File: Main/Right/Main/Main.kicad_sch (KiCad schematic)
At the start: 44 parts, among them SW1 RotaryEncoder_Switch_MP, SW2 Switch, U1 Arduino_Pro_Micro, U2 TRRS

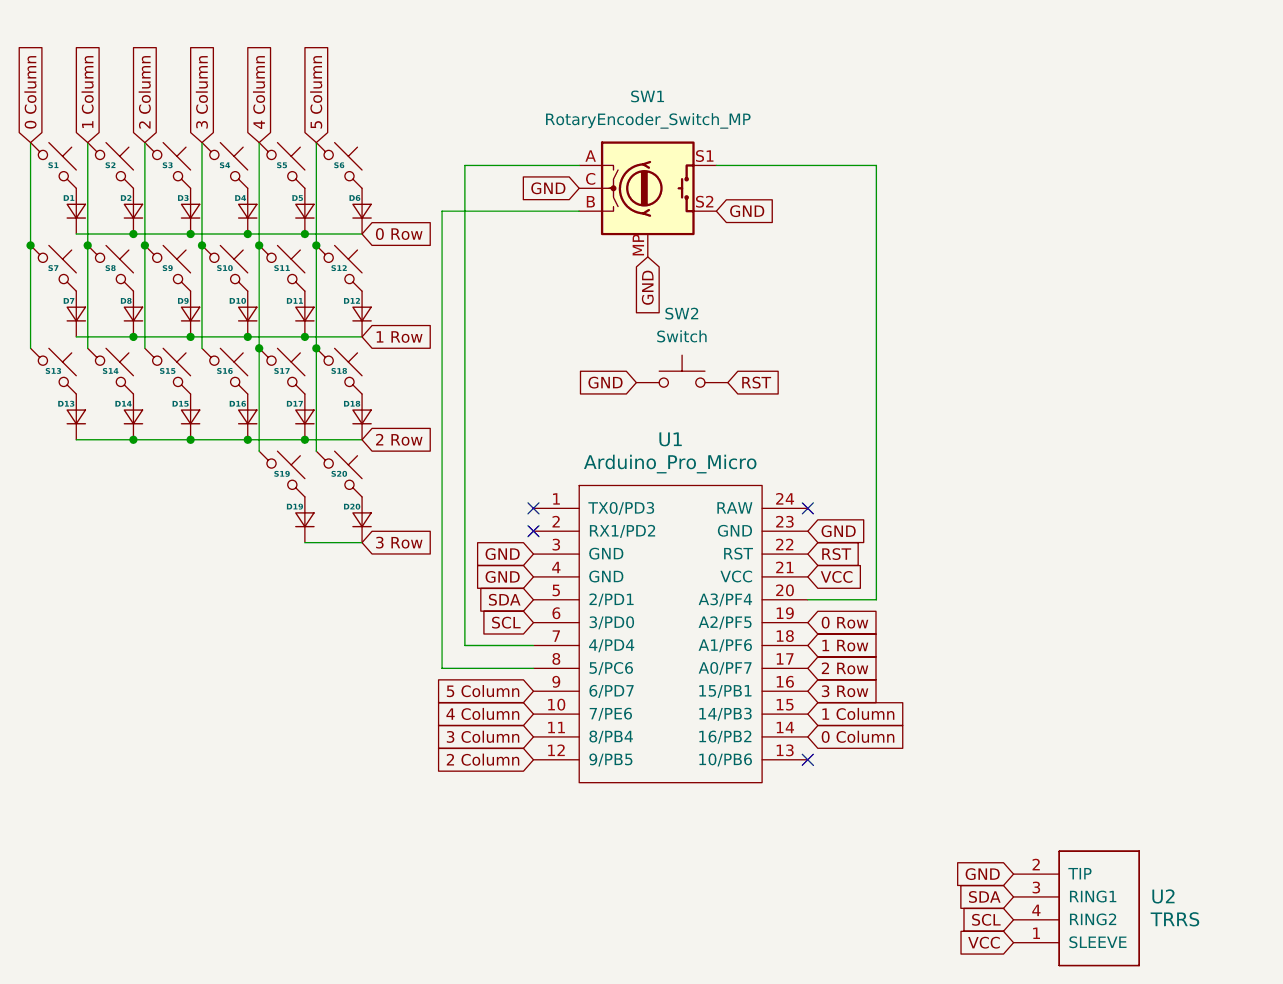
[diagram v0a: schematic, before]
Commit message: changed from I2C communication between the halves to serial because it's easier with QMK
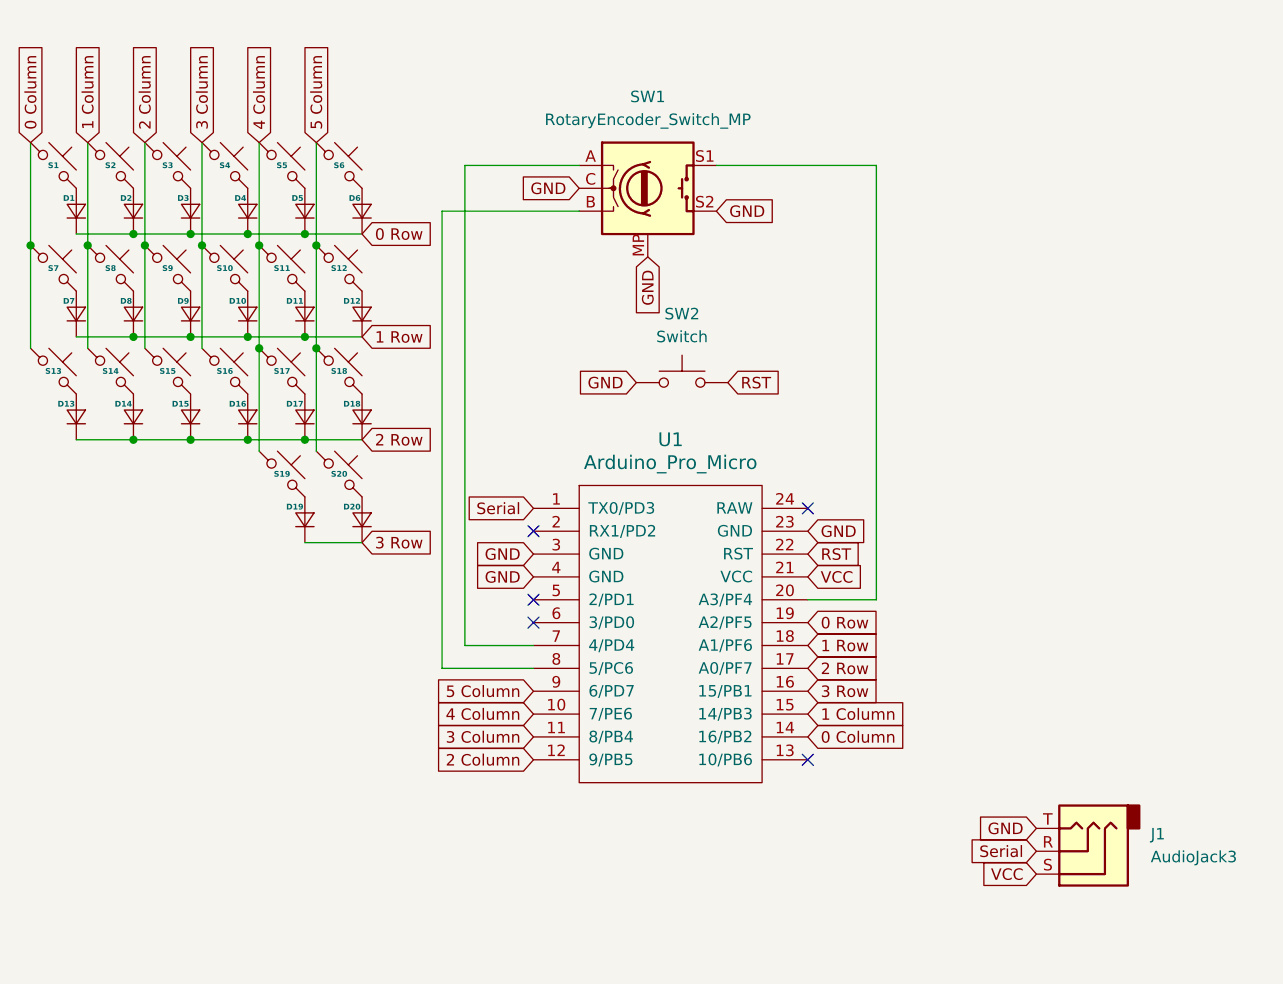
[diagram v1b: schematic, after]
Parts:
- removed U2: TRRS, ScottoKeebs_Components:TRRS_PJ-320A, symbol ScottoKeebs:Placeholder_TRRS
- added J1: AudioJack3, Connector_Audio:Jack_3.5mm_CUI_SJ1-3533NG_Horizontal_CircularHoles, symbol Connector_Audio:AudioJack3
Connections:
- net GND: now also J1.T
- net VCC: now also J1.S
- net Serial: now reaches U1.1 (TX0/PD3)
- net Serial: now also J1.R
- net SCL: no longer names the net of U1.6 (3/PD0)
- net SDA: no longer names the net of U1.5 (2/PD1)
- no-connect marks 4 -> 5
